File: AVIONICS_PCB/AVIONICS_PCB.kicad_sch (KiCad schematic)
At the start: 22 parts, among them IC1 MMBT2222ALT1G, IC2 MMBT2222ALT1G, J1 XT30PW-M, J2 Screw_Terminal_01x02, J3 Screw_Terminal_01x02, J4 Conn_01x03, J5 Conn_01x03, J6 Conn_01x03, J7 Conn_01x03, U1 ESP32-S3-DevKitC

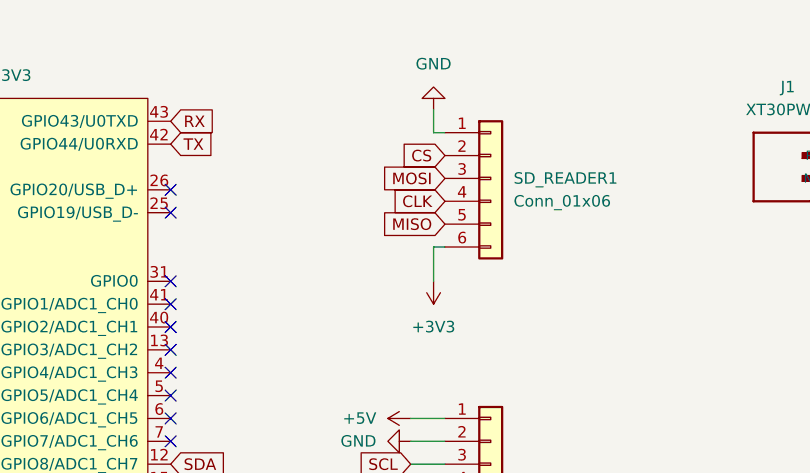
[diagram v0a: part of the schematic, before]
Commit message: SD testing
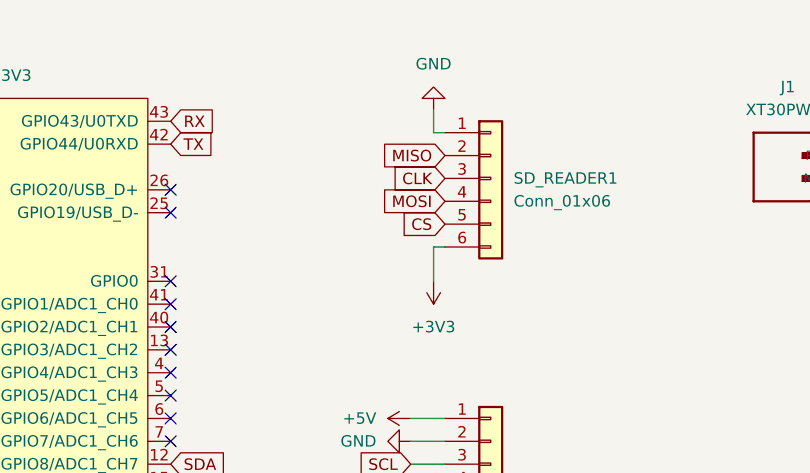
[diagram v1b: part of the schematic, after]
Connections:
- net CLK: now also SD_READER1.3 (Pin_3); no longer SD_READER1.4 (Pin_4)
- net CS: now also SD_READER1.5 (Pin_5); no longer SD_READER1.2 (Pin_2)
- net MISO: now also SD_READER1.2 (Pin_2); no longer SD_READER1.5 (Pin_5)
- net MOSI: now also SD_READER1.4 (Pin_4); no longer SD_READER1.3 (Pin_3)

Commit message: working on v3
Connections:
- net servo1: now also U1.31 (GPIO0); no longer U1.35 (GPIO38)
- net servo2: no longer U1.34 (GPIO37)
- net servo3: no longer U1.33 (GPIO36)
- net servo4: no longer U1.32 (GPIO35)
- no-connect marks 27 -> 30
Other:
- note added: "35/36/37 Not Available"
